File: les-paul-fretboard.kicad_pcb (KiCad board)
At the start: 2 copper layers, 155 x 25 mm, 15 parts, among them J1 Conn_01x10_Female, J2 Conn_01x10_Female, SW1 Green(A), SW2 Red(B), SW3 Yellow(Y), SW4 Blue(X), SW5 Orange(TB), U1 SN74LV1T34DBV

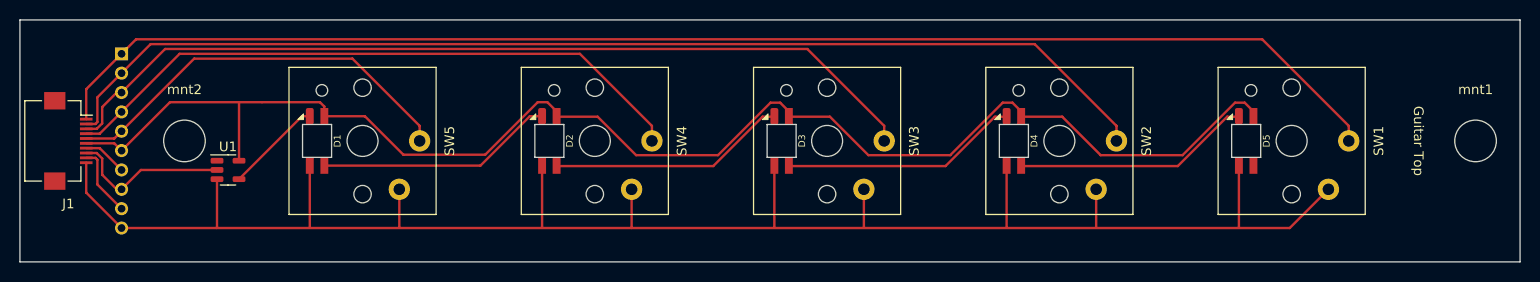
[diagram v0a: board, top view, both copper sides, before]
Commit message: Replace LED footprint with intended footprint (pin layout was wrong)
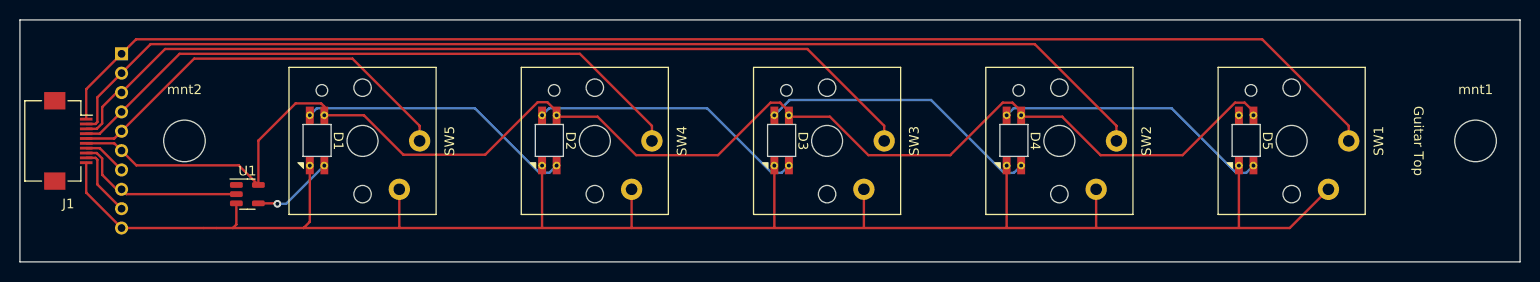
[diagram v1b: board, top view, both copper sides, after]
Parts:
- D1, D2, D3, D4, D5: footprint Keebio-Parts:SK6812-MINI-E -> SK6812MINI-E:SK6812MINI-E-Vias
- moved U1 3.20 mm to (84.0, 92.0)
- turned D1 to -90 degrees
- turned D2 to -90 degrees
- turned D3 to -90 degrees
- turned D4 to -90 degrees
- turned D5 to -90 degrees
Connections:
- D1 pad 1: Net-(D1-Pad1) -> +5V
- D1 pad 2: GND -> Net-(D1-Pad2)
- D1 pad 3: Net-(D1-Pad3) -> GND
- D1 pad 4: +5V -> Net-(D1-Pad4)
- D2 pad 1: Net-(D2-Pad1) -> +5V
- D2 pad 2: GND -> Net-(D2-Pad2)
- D2 pad 3: Net-(D1-Pad1) -> GND
- D2 pad 4: +5V -> Net-(D1-Pad2)
- D3 pad 1: Net-(D3-Pad1) -> +5V
- D3 pad 2: GND -> Net-(D3-Pad2)
- D3 pad 3: Net-(D2-Pad1) -> GND
- D3 pad 4: +5V -> Net-(D2-Pad2)
- D4 pad 1: Net-(D4-Pad1) -> +5V
- D4 pad 2: GND -> Net-(D4-Pad2)
- D4 pad 3: Net-(D3-Pad1) -> GND
- D4 pad 4: +5V -> Net-(D3-Pad2)
- D5 pad 1: unconnected-(D5-Pad1) -> +5V
- D5 pad 2: GND -> unconnected-(D5-Pad2)
- D5 pad 3: Net-(D4-Pad1) -> GND
- D5 pad 4: +5V -> Net-(D4-Pad2)
- U1 pad 4: Net-(D1-Pad3) -> Net-(D1-Pad4)
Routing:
- net Net-(D3-Pad2): track 0.00 -> 29.6 mm
- net Net-(D4-Pad2): track 0.00 -> 28.9 mm
- net Net-(D2-Pad2): track 0.00 -> 28.9 mm
- net Net-(D1-Pad2): track 0.00 -> 28.9 mm
- net Net-(D4-Pad1): track 24.6 -> 0.00 mm
- net Net-(D3-Pad1): track 24.6 -> 0.00 mm
- net Net-(D2-Pad1): track 24.6 -> 0.00 mm
- net Net-(D1-Pad1): track 24.6 -> 0.00 mm
- net Net-(D1-Pad3): track 10.0 -> 0.00 mm
- net Net-(D1-Pad4): track 0.00 -> 8.96 mm, vias 0 -> 1
- net GND: track 187.6 -> 185.6 mm
- net /SDA: track 16.9 -> 18.3 mm
